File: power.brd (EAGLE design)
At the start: 90.2 x 95.9 mm, 65 parts, among them J1 POWER_JACKPTH_BREAD, T1 SINGLE_NCHAN_FET, T2 SINGLE_NCHAN_FET, T3 SINGLE_NCHAN_FET, U1 MOSFET_PCHAN_20A, U14 MOSFET_PCHAN_20A, U2 MOSFET_PCHAN_20A

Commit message: Changed to all sparkfun library parts
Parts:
- C12, C13, C30, C31, C32: device phonesat:0805 -> SparkFun-Capacitors:0805
- R2, R27, R28, R3, R5, R6, R7, R8: device phonesat:0805 -> SparkFun-Resistors:0805
- moved R8 241.6 mm to (38.8, 45.7), turned to 90 degrees
- moved C13 236.7 mm to (35.0, 45.7), turned to 90 degrees
- moved U$15 236.7 mm to (15.3, 56.7), turned to 90 degrees
- moved JP4 233.7 mm to (85.1, 57.8), turned to 270 degrees
- moved JP5 230.8 mm to (85.0, 46.7), turned to 270 degrees
- moved U$14 228.3 mm to (21.6, 58.2), turned to 90 degrees
- moved R5 225.5 mm to (26.3, 45.7), turned to 90 degrees
- moved C12 220.7 mm to (22.6, 45.7), turned to 90 degrees
- moved C11 212.9 mm to (50.3, 60.4)
- moved R4 207.7 mm to (12.2, 46.2), turned to 90 degrees
- moved D1 202.1 mm to (31.9, 63.0)
- moved R1 201.2 mm to (7.04, 46.2), turned to 90 degrees
- moved D2 200.8 mm to (49.6, 51.8)
- moved R13 198.0 mm to (58.6, 47.2)
- moved C10 194.7 mm to (44.2, 44.5)
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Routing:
- added copper zone on layer 16, net N$1

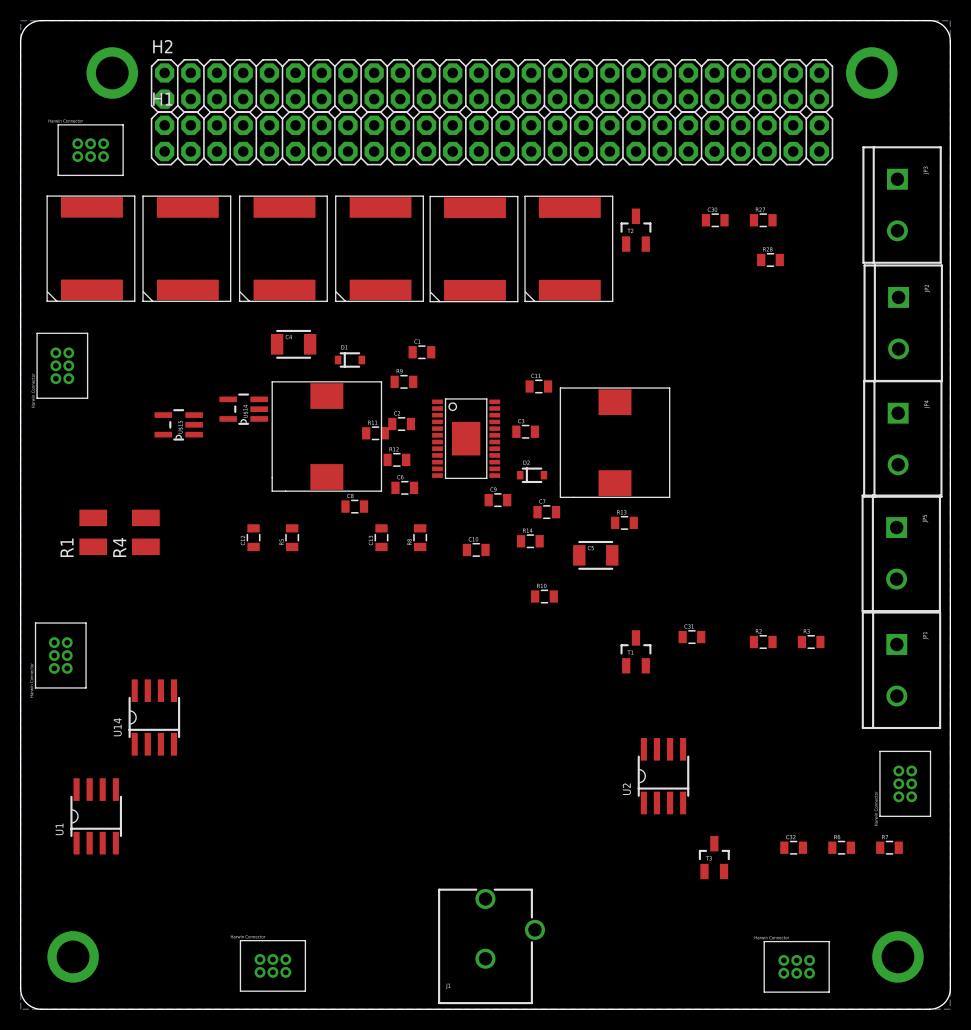
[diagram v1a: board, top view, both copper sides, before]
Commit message: Board layout for switching regulator
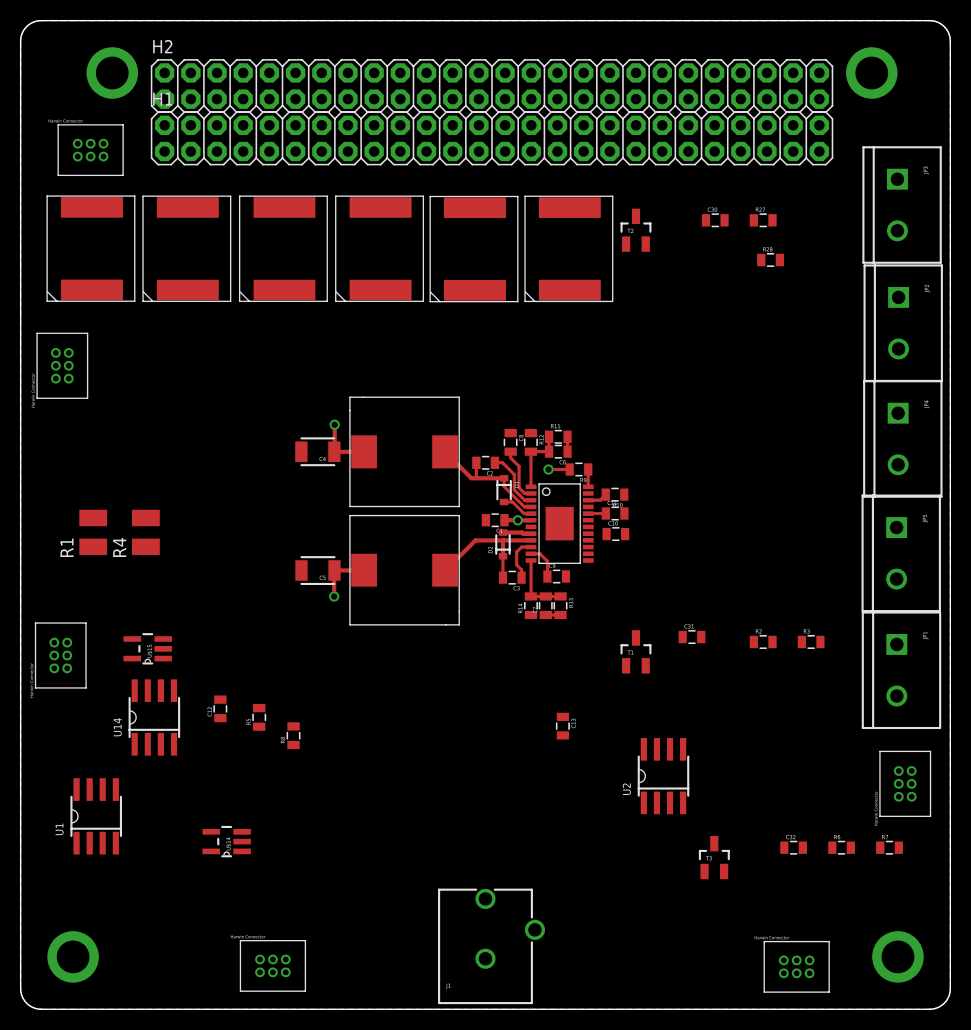
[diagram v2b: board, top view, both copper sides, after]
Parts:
- moved U$14 42.0 mm to (20.0, 16.3)
- moved C5 27.0 mm to (28.8, 42.5), turned to 180 degrees
- moved C13 25.4 mm to (52.6, 27.5), turned to 270 degrees
- moved L2 23.9 mm to (37.2, 42.6), turned to 180 degrees
- moved R8 22.8 mm to (26.5, 26.5)
- moved U$15 21.9 mm to (12.3, 35.0)
- moved D1 19.6 mm to (46.9, 50.4), turned to 270 degrees
- moved R9 19.0 mm to (54.1, 52.4), turned to 180 degrees
- moved C1 17.8 mm to (46.0, 47.4), turned to 180 degrees
- moved R11 17.7 mm to (52.1, 55.5)
- moved R5 17.7 mm to (23.1, 28.3)
- moved C12 16.9 mm to (19.4, 29.1)
- moved C8 16.3 mm to (47.5, 55.0), turned to 270 degrees
- moved C6 15.3 mm to (52.1, 54.1), turned to 180 degrees
- moved C11 14.4 mm to (57.7, 48.1)
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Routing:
- net N$15: track 0.00 -> 13.2 mm
- net N$10: track 0.00 -> 12.6 mm
- net VREG_IN: track 0.00 -> 10.8 mm, vias 0 -> 2
- net 5V: track 0.00 -> 7.06 mm, vias 0 -> 1
- net 3.3V: track 0.00 -> 6.96 mm, vias 0 -> 1
- net N$12: track 0.00 -> 6.61 mm
- net N$14: track 0.00 -> 6.35 mm
- net N$9: track 0.00 -> 5.89 mm
- net N$13: track 0.00 -> 5.24 mm
- net N$11: track 0.00 -> 4.28 mm
- net N$8: track 0.00 -> 3.37 mm
- net N$16: track 0.00 -> 3.08 mm
- net N$17: track 0.00 -> 2.77 mm
- net N$18: track 0.00 -> 1.92 mm
- net N$22: track 0.00 -> 1.71 mm
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- added copper zone on layer 2, net 3.3V
- added copper zone on layer 15, net 5V
- added copper zone on layer 1, net GND

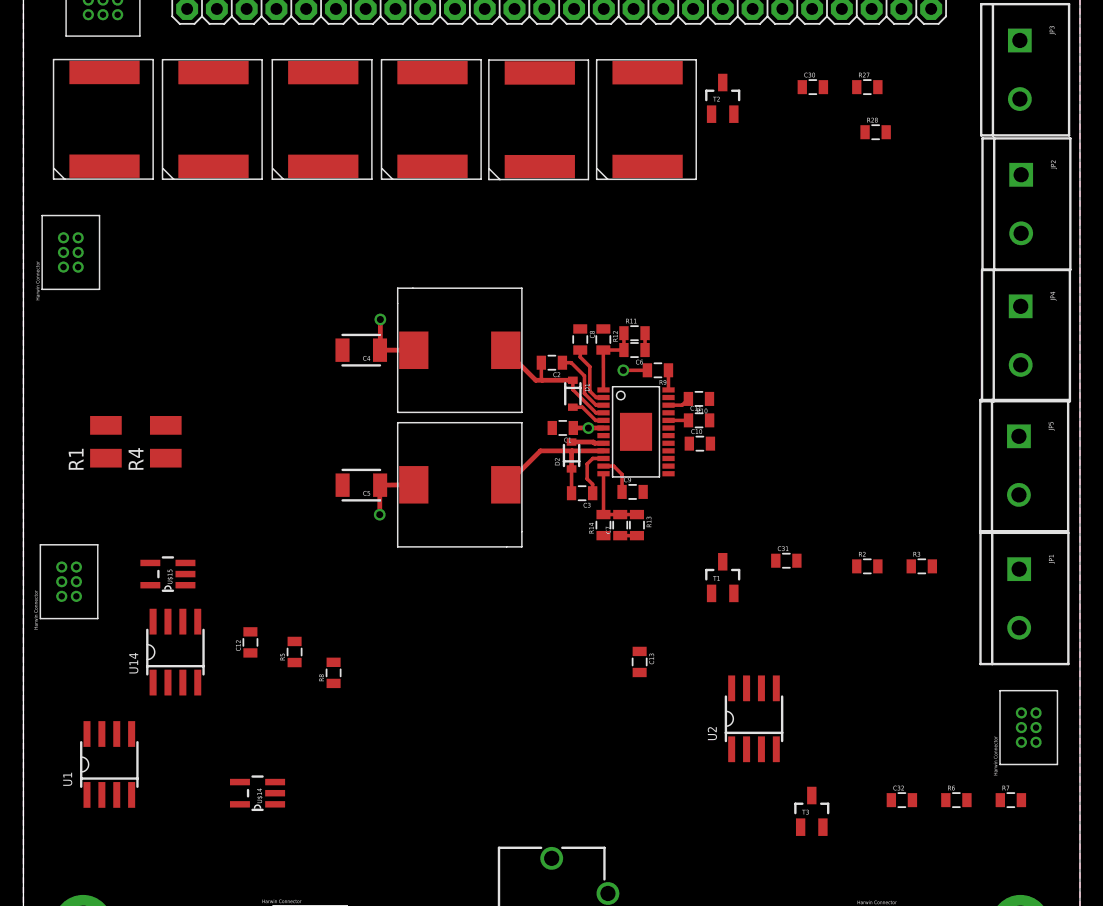
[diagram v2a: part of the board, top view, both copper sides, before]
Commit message: More power board layout work
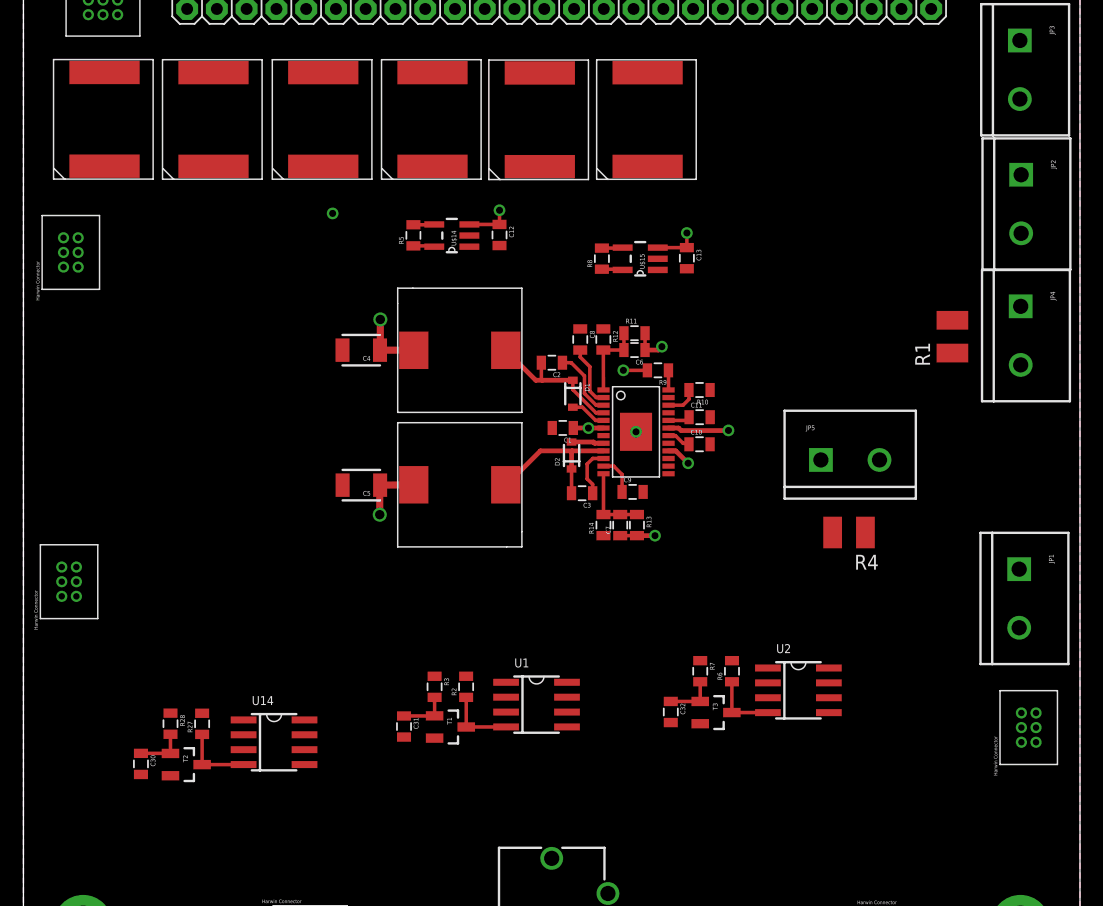
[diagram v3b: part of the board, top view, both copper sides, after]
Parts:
- moved C30 81.4 mm to (10.0, 18.8), turned to 270 degrees
- moved R27 78.6 mm to (15.2, 22.2), turned to 90 degrees
- moved R28 78.5 mm to (12.6, 22.2), turned to 270 degrees
- moved T2 73.0 mm to (13.8, 18.7), turned to 270 degrees
- moved R1 72.8 mm to (79.3, 55.2)
- moved R4 58.8 mm to (70.5, 38.5), turned to 180 degrees
- moved U$14 50.4 mm to (36.6, 63.9)
- moved U$15 48.5 mm to (52.6, 61.9)
- moved R3 42.8 mm to (35.1, 25.3), turned to 270 degrees
- moved R8 42.1 mm to (49.4, 61.9)
- moved C12 40.8 mm to (40.6, 63.9), turned to 270 degrees
- moved R5 37.0 mm to (33.3, 63.9)
- moved U1 36.8 mm to (43.8, 23.8), turned to 270 degrees
- moved R2 35.7 mm to (37.8, 25.3), turned to 90 degrees
- moved C31 35.6 mm to (32.5, 21.9), turned to 270 degrees
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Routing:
- net 3.3V: track 6.96 -> 21.3 mm, vias 1 -> 5
- net N$24: track 0.00 -> 6.12 mm
- net N$3: track 0.00 -> 5.93 mm
- net N$6: track 0.00 -> 5.72 mm
- net N$2: track 0.00 -> 4.19 mm
- net N$5: track 0.00 -> 4.19 mm
- net N$21: track 0.00 -> 4.16 mm
- net 5V: track 7.06 -> 10.8 mm, vias 1 -> 3
- net VBATT: track 0.00 -> 3.60 mm
- net N$20: track 0.00 -> 2.05 mm
- net VREG_IN: track 10.8 -> 12.6 mm
- net VSOLAR: track 0.00 -> 1.79 mm
- net N$18: track 1.92 -> 2.74 mm

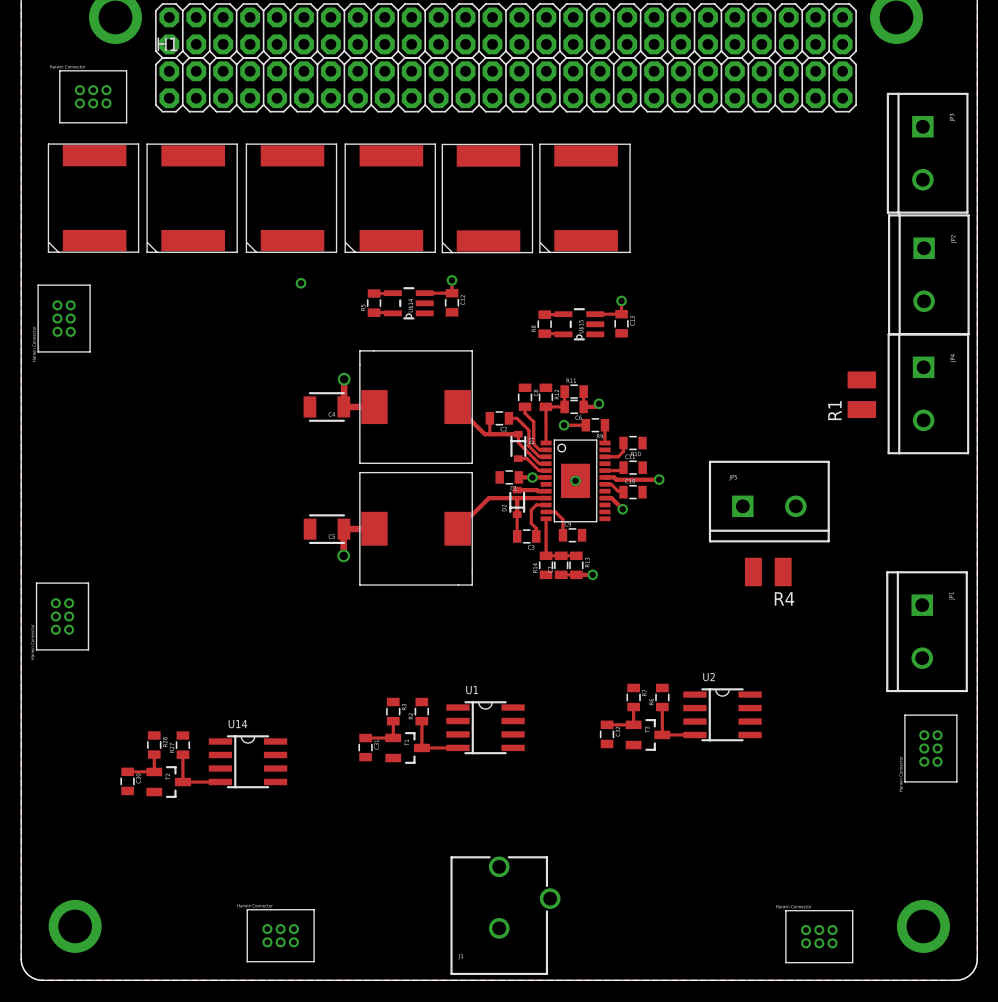
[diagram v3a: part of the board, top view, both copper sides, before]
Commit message: Added breakout for USB and charging
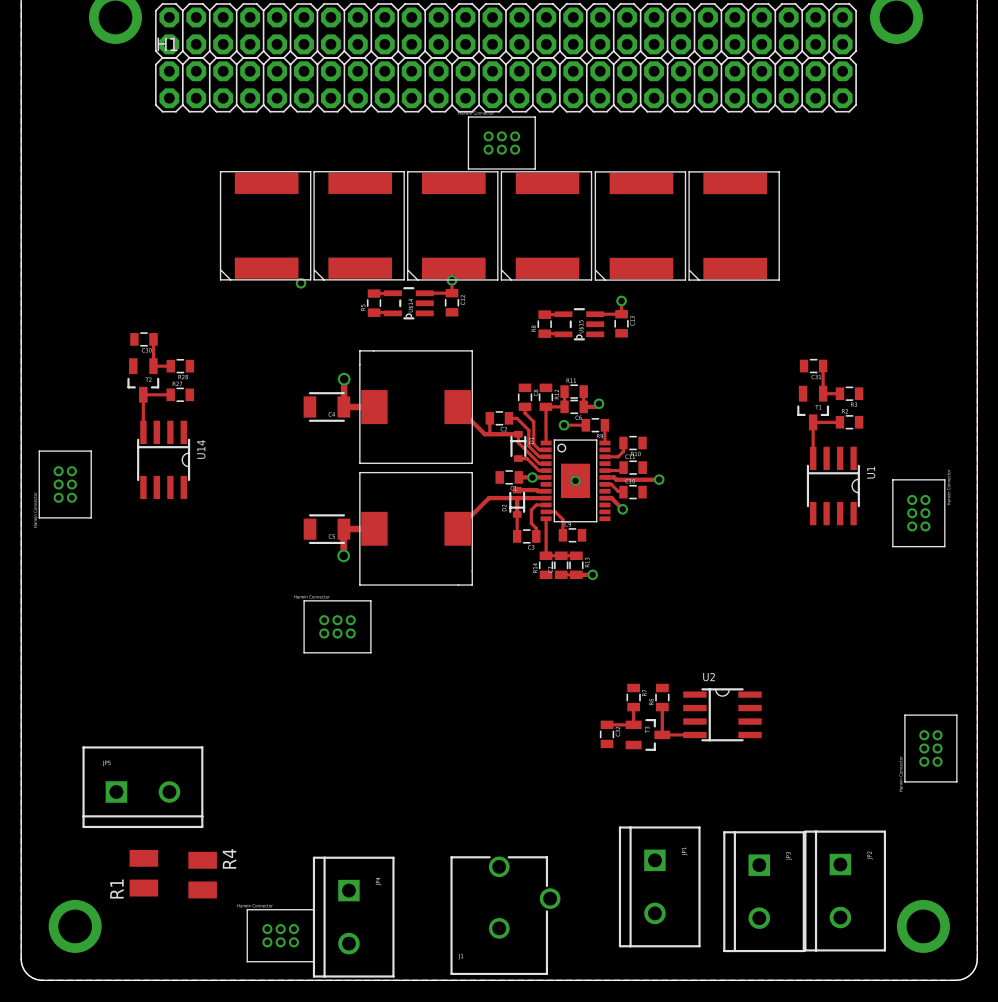
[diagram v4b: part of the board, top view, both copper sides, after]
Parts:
- moved R1 81.4 mm to (11.6, 10.1)
- moved U$1 76.5 mm to (82.1, 47.2), turned to 270 degrees
- moved JP4 73.3 mm to (30.9, 8.46)
- moved JP3 71.3 mm to (69.6, 10.9)
- moved JP5 64.9 mm to (8.98, 17.8)
- moved R4 60.5 mm to (17.1, 9.92), turned to 270 degrees
- moved JP2 58.7 mm to (77.3, 10.9)
- moved U$3 57.7 mm to (42.1, 76.4), turned to 0 degrees
- moved C31 55.5 mm to (74.7, 57.9), turned to 180 degrees
- moved U$5 54.0 mm to (26.6, 30.8)
- moved R3 52.4 mm to (78.1, 55.3), turned to 180 degrees
- moved T1 50.0 mm to (74.7, 54.0), turned to 180 degrees
- moved R2 48.7 mm to (78.1, 52.6), turned to 0 degrees
- moved C30 41.7 mm to (11.6, 60.4), turned to 180 degrees
- moved U1 40.0 mm to (76.6, 46.6), turned to 180 degrees
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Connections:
- net VSOLAR: now also U$1.P3, U$1.P6, U$2.P3, U$2.P6, U$3.P3, U$3.P6, U$4.P3, U$4.P6, U$6.P3, U$6.P6
